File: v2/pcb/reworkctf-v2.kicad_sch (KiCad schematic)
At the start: 68 parts, among them J16 TESTPOINT, J17 TESTPOINT, J2 CORTEX_DEBUG_ETM, J3 DOT, J4 TESTPOINT, J6 CONN_01X03, J7 PMOD_HOST, J8 PMOD_HOST, M1 SCREWHOLE, M2 SCREWHOLE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

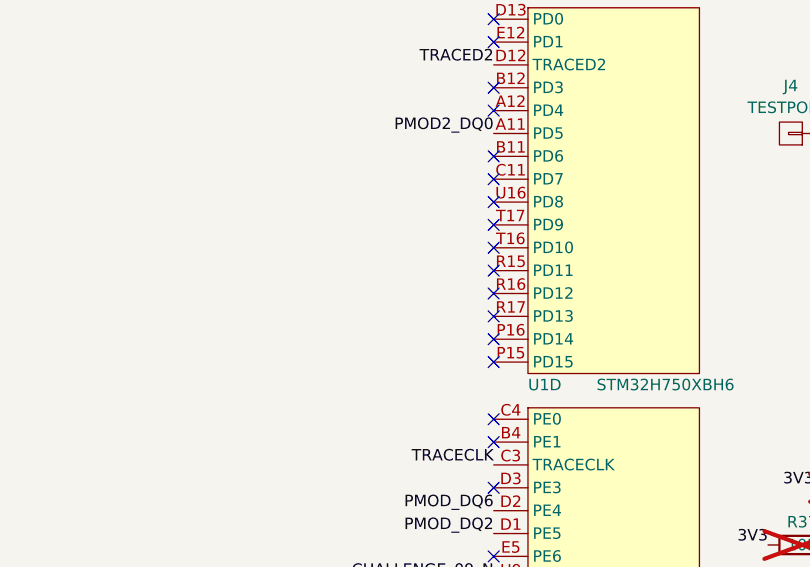
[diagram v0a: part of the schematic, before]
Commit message: Added strap via to wrong net. Should be ready to order, I think
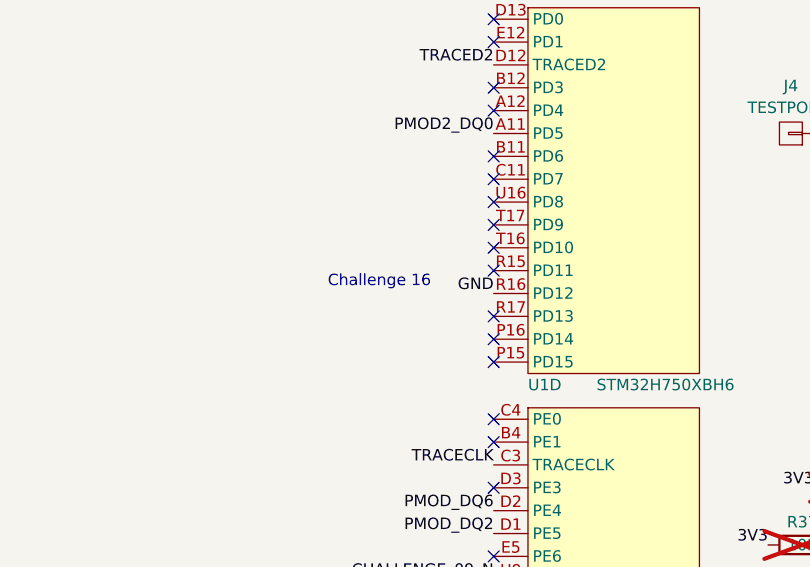
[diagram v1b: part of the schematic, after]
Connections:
- net GND: now also U1.R16 (PD12)
- no-connect marks 101 -> 100
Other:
- note added: "Challenge 16"
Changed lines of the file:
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@@
 	(generator_version "9.0")
 	(paper "A3")
+	(text "Challenge 16"
+		(exclude_from_sim no)
+		(at 96.52 195.58 0)
+		(effects
+			(font
+				(size 1.27 1.27)
+			)
+		)
+	)
 	(text "GPIO expansion\nfor use as devkit\nafter challenge\nis complete"
 		(exclude_from_sim no)
@@
 	)
 	(no_connect
+		(at 109.22 189.23)
+	)
+	(no_connect
 		(at 109.22 210.82)
 	)
@@
 	)
 	(no_connect
-		(at 109.22 196.85)
-	)
-	(no_connect
 		(at 166.37 210.82)
 	)
@@
 	(no_connect
 		(at 166.37 129.54)
-	)
-	(no_connect
-		(at 109.22 189.23)
 	)
 	(no_connect
@@
 		(effects
 			(font
+				(size 1.27 1.27)
+			)
+			(justify right bottom)
+		)
+	)
+	(label "GND"
+		(at 109.22 196.85 180)
+		(effects
+			(font
